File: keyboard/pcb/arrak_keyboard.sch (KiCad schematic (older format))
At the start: 40 parts, among them SW1 SW_PUSH, SW10 SW_PUSH, SW11 SW_PUSH, SW12 SW_PUSH, SW13 SW_PUSH, SW14 SW_PUSH, SW15 SW_PUSH, SW16 SW_PUSH, SW17 SW_PUSH, SW18 SW_PUSH, SW19 SW_PUSH, SW2 SW_PUSH, SW20 SW_PUSH, SW21 SW_PUSH, SW22 SW_PUSH, SW23 SW_PUSH, SW24 SW_PUSH, SW25 SW_PUSH, SW26 SW_PUSH, SW27 SW_PUSH, SW28 SW_PUSH, SW29 SW_PUSH, SW3 SW_PUSH, SW30 SW_PUSH, SW31 SW_PUSH, SW32 SW_PUSH, SW33 SW_PUSH, SW34 SW_PUSH, SW35 SW_PUSH, SW36 SW_PUSH, SW4 SW_PUSH, SW5 SW_PUSH, SW6 SW_PUSH, SW7 SW_PUSH, SW8 SW_PUSH, SW9 SW_PUSH

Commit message: weird routing
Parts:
- gave numbers to parts that had none: 4
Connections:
- net D10: now also J1.7 (Pin_7); no longer J1.9 (Pin_9)
- net D11: now also J1.15 (Pin_15); no longer J1.8 (Pin_8)
- net D12: now also J1.10 (Pin_10); no longer J1.7 (Pin_7)
- net D13: now also J1.5 (Pin_5); no longer J1.6 (Pin_6)
- net D14: now also J1.8 (Pin_8); no longer J1.5 (Pin_5)
- net D15: now also J1.14 (Pin_14); no longer J1.4 (Pin_4)
- net D17: now also J1.6 (Pin_6); no longer J1.2 (Pin_2)
- net D18: now also J1.9 (Pin_9); no longer J1.1 (Pin_1)
- net D19: now also J2.14 (Pin_14), SW19.2; no longer J2.18 (Pin_18), SW34.2
- net D2: now also J1.13 (Pin_13); no longer J1.17 (Pin_17)
- net D20: now also J2.10 (Pin_10), SW20.2; no longer J2.17 (Pin_17), SW35.2
- net D21: now also J2.6 (Pin_6), SW21.2; no longer J2.16 (Pin_16), SW36.2
- net D22: now also J2.3 (Pin_3), SW22.2; no longer J2.15 (Pin_15), SW31.2
- net D23: now also J2.15 (Pin_15), SW23.2; no longer J2.14 (Pin_14), SW32.2
- net D24: now also SW24.2; no longer SW33.2
- net D25: now also SW25.2; no longer SW27.2
- net D26: now also SW26.2; no longer SW28.2
- net D27: now also J2.16 (Pin_16), SW27.2; no longer J2.10 (Pin_10), SW29.2
- net D28: now also SW28.2; no longer SW30.2
- net D29: now also SW29.2; no longer SW23.2
- net D3: now also J1.1 (Pin_1); no longer J1.16 (Pin_16)
- net D30: now also SW30.2; no longer SW24.2
- net D31: now also J2.17 (Pin_17), SW31.2; no longer J2.6 (Pin_6), SW25.2
- net D32: now also SW32.2; no longer SW26.2
- net D33: now also SW33.2; no longer SW19.2
- net D34: now also J2.18 (Pin_18), SW34.2; no longer J2.3 (Pin_3), SW20.2
- net D35: now also SW35.2; no longer SW21.2
- net D36: now also SW36.2; no longer SW22.2
- net D4: now also J1.17 (Pin_17); no longer J1.15 (Pin_15)
- net D5: now also J1.12 (Pin_12); no longer J1.14 (Pin_14)
- net D6: now also J1.2 (Pin_2); no longer J1.13 (Pin_13)
- net D7: now also J1.16 (Pin_16); no longer J1.12 (Pin_12)
- net D9: now also J1.4 (Pin_4); no longer J1.10 (Pin_10)

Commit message: lite bättre routing
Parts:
- removed J3, J4: Conn_01x02_Male, symbol Connector:Conn_01x02_Male
- J1: value Conn_01x18_Male -> Conn_01x20_Male; symbol Connector:Conn_01x18_Male -> Connector:Conn_01x20_Male
- J2: value Conn_01x18_Male -> Conn_01x20_Male; footprint (none) -> Connector_PinHeader_2.54mm:PinHeader_1x20_P2.54mm_Vertical; symbol Connector:Conn_01x18_Male -> Connector:Conn_01x20_Male
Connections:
- net D16: now also J1.2 (Pin_2); no longer J1.3 (Pin_3)
- net D20: now also J2.5 (Pin_5); no longer J2.10 (Pin_10)
- net D22: now also J2.9 (Pin_9); no longer J2.3 (Pin_3)
- net D24: now also J2.10 (Pin_10); no longer J2.13 (Pin_13)
- net D25: now also J2.4 (Pin_4); no longer J2.12 (Pin_12)
- net D26: now also J2.8 (Pin_8); no longer J2.11 (Pin_11)
- net D28: now also J2.11 (Pin_11); no longer J2.9 (Pin_9)
- net D29: now also J2.3 (Pin_3); no longer J2.8 (Pin_8)
- net D32: now also J2.12 (Pin_12); no longer J2.5 (Pin_5)
- net D33: now also J2.2 (Pin_2); no longer J2.4 (Pin_4)
- net D35: now also J2.13 (Pin_13); no longer J2.2 (Pin_2)
- net D6: now also J1.3 (Pin_3); no longer J1.2 (Pin_2)
- net R1: now also J1.20 (Pin_20)
- net R2: now also J1.19 (Pin_19)
- net R3: now also J2.20 (Pin_20)
- net R4: now also J2.19 (Pin_19)
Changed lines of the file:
@@
 Text GLabel 4150 2200 0    50   Input ~ 0
 R4
-Text GLabel 7300 1150 3    50   Input ~ 0
+Text GLabel 5100 1150 3    50   Input ~ 0
 R1
-Text GLabel 7400 1150 3    50   Input ~ 0
+Text GLabel 5200 1150 3    50   Input ~ 0
 R2
-Text GLabel 7300 3000 3    50   Input ~ 0
+Text GLabel 5000 3050 3    50   Input ~ 0
 R3
-Text GLabel 7400 3000 3    50   Input ~ 0
+Text GLabel 5100 3050 3    50   Input ~ 0
 R4
-Text GLabel 5100 1150 3    50   Input ~ 0
+Text GLabel 5300 1150 3    50   Input ~ 0
 D1
+Text GLabel 5800 1150 3    50   Input ~ 0
+D2
+Text GLabel 7000 1150 3    50   Input ~ 0
+D3
+Text GLabel 5400 1150 3    50   Input ~ 0
+D4
+Text GLabel 5900 1150 3    50   Input ~ 0
+D5
+Text GLabel 5500 1150 3    50   Input ~ 0
+D7
+Text GLabel 6000 1150 3    50   Input ~ 0
+D8
+Text GLabel 6700 1150 3    50   Input ~ 0
+D9
+Text GLabel 6400 1150 3    50   Input ~ 0
+D10
 Text GLabel 5600 1150 3    50   Input ~ 0
-D2
-Text GLabel 6800 1150 3    50   Input ~ 0
-D3
-Text GLabel 5200 1150 3    50   Input ~ 0
-D4
+D11
+Text GLabel 6100 1150 3    50   Input ~ 0
+D12
+Text GLabel 6600 1150 3    50   Input ~ 0
+D13
+Text GLabel 6300 1150 3    50   Input ~ 0
+D14
 Text GLabel 5700 1150 3    50   Input ~ 0
-D5
-Text GLabel 5300 1150 3    50   Input ~ 0
-D7
-Text GLabel 5800 1150 3    50   Input ~ 0
-D8
+D15
+Text GLabel 6900 1150 3    50   Input ~ 0
+D16
 Text GLabel 6500 1150 3    50   Input ~ 0
-D9
+D17
 Text GLabel 6200 1150 3    50   Input ~ 0
-D10
-Text GLabel 5400 1150 3    50   Input ~ 0
-D11
-Text GLabel 5900 1150 3    50   Input ~ 0
-D12
-Text GLabel 6400 1150 3    50   Input ~ 0
-D13
-Text GLabel 6100 1150 3    50   Input ~ 0
-D14
-Text GLabel 5500 1150 3    50   Input ~ 0
-D15
-Text GLabel 6600 1150 3    50   Input ~ 0
-D16
-Text GLabel 6300 1150 3    50   Input ~ 0
-D17
-Text GLabel 6000 1150 3    50   Input ~ 0
 D18
 Entry Wire Line
@@
 Text GLabel 2500 4100 0    50   Input ~ 0
 R4
-Text GLabel 6700 1150 3    50   Input ~ 0
+Text GLabel 6800 1150 3    50   Input ~ 0
 D6
 $Comp
-L Connector:Conn_01x18_Male J1
+L Connector:Conn_01x20_Male J1
 U 1 1 6117D25B
-P 6000 950
-F 0 "J1" V 5835 878 50  0000 C CNN
-F 1 "Conn_01x18_Male" V 5926 878 50  0000 C CNN
-F 2 "" H 6000 950 50  0001 C CNN
-F 3 "~" H 6000 950 50  0001 C CNN
-	1    6000 950
+P 6100 950
+F 0 "J1" V 5935 878 50  0000 C CNN
+F 1 "Conn_01x20_Male" V 6026 878 50  0000 C CNN
+F 2 "" H 6100 950 50  0001 C CNN
+F 3 "~" H 6100 950 50  0001 C CNN
+	1    6100 950
 	0    1    1    0
 $EndComp
 $Comp
-L Connector:Conn_01x18_Male J2
+L Connector:Conn_01x20_Male J2
 U 1 1 6117F46E
 P 6000 2850
 F 0 "J2" V 5835 2778 50  0000 C CNN
-F 1 "Conn_01x18_Male" V 5926 2778 50  0000 C CNN
-F 2 "" H 6000 2850 50  0001 C CNN
+F 1 "Conn_01x20_Male" V 5926 2778 50  0000 C CNN
+F 2 "Connector_PinHeader_2.54mm:PinHeader_1x20_P2.54mm_Vertical" H 6000 2850 50  0001 C CNN
 F 3 "~" H 6000 2850 50  0001 C CNN
 	1    6000 2850
-	0    1    1    0
-$EndComp
-$Comp
-L Connector:Conn_01x02_Male J3
-U 1 1 61180CFF
-P 7400 950
-F 0 "J3" V 7462 994 50  0000 L CNN
-F 1 "Conn_01x02_Male" V 7553 994 50  0000 L CNN
-F 2 "" H 7400 950 50  0001 C CNN
-F 3 "~" H 7400 950 50  0001 C CNN
-	1    7400 950
-	0    1    1    0
-$EndComp
-$Comp
-L Connector:Conn_01x02_Male J4
-U 1 1 6118151C
-P 7400 2800
-F 0 "J4" V 7462 2844 50  0000 L CNN
-F 1 "Conn_01x02_Male" V 7553 2844 50  0000 L CNN
-F 2 "" H 7400 2800 50  0001 C CNN
-F 3 "~" H 7400 2800 50  0001 C CNN
-	1    7400 2800
 	0    1    1    0
 $EndComp
@@
 Text GLabel 4800 3700 3    50   Input ~ 0
 D36
+Text GLabel 5600 3050 3    50   Input ~ 0
+D19
+Text GLabel 6500 3050 3    50   Input ~ 0
+D20
+Text GLabel 6400 3050 3    50   Input ~ 0
+D21
+Text GLabel 6100 3050 3    50   Input ~ 0
+D22
 Text GLabel 5500 3050 3    50   Input ~ 0
-D19
+D23
+Text GLabel 6000 3050 3    50   Input ~ 0
+D24
+Text GLabel 6600 3050 3    50   Input ~ 0
+D25
+Text GLabel 6200 3050 3    50   Input ~ 0
+D26
+Text GLabel 5400 3050 3    50   Input ~ 0
+D27
 Text GLabel 5900 3050 3    50   Input ~ 0
-D20
+D28
+Text GLabel 6700 3050 3    50   Input ~ 0
+D29
 Text GLabel 6300 3050 3    50   Input ~ 0
-D21
-Text GLabel 6600 3050 3    50   Input ~ 0
-D22
-Text GLabel 5400 3050 3    50   Input ~ 0
-D23
-Text GLabel 5600 3050 3    50   Input ~ 0
-D24
+D30
+Text GLabel 5300 3050 3    50   Input ~ 0
+D31
+Text GLabel 5800 3050 3    50   Input ~ 0
+D32
+Text GLabel 6800 3050 3    50   Input ~ 0
+D33
+Text GLabel 5200 3050 3    50   Input ~ 0
+D34
 Text GLabel 5700 3050 3    50   Input ~ 0
-D25
-Text GLabel 5800 3050 3    50   Input ~ 0
-D26
-Text GLabel 5300 3050 3    50   Input ~ 0
-D27
-Text GLabel 6000 3050 3    50   Input ~ 0
-D28
-Text GLabel 6100 3050 3    50   Input ~ 0
-D29
-Text GLabel 6200 3050 3    50   Input ~ 0
-D30
-Text GLabel 5200 3050 3    50   Input ~ 0
-D31
-Text GLabel 6400 3050 3    50   Input ~ 0
-D32
-Text GLabel 6500 3050 3    50   Input ~ 0
-D33
-Text GLabel 5100 3050 3    50   Input ~ 0
-D34
-Text GLabel 6700 3050 3    50   Input ~ 0
 D35
-Text GLabel 6800 3050 3    50   Input ~ 0
+Text GLabel 6900 3050 3    50   Input ~ 0
 D36
 $Comp

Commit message: finish keyboard pcb
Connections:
- net D10: now also J1.9 (Pin_9); no longer J1.7 (Pin_7)
- net D11: now also J1.5 (Pin_5); no longer J1.15 (Pin_15)
- net D12: now also J1.6 (Pin_6); no longer J1.10 (Pin_10)
- net D13: now also J1.7 (Pin_7); no longer J1.5 (Pin_5)
- net D15: now also J1.1 (Pin_1); no longer J1.14 (Pin_14)
- net D17: now also J1.3 (Pin_3); no longer J1.6 (Pin_6)
- net D18: now also J1.4 (Pin_4); no longer J1.9 (Pin_9)
- net D19: now also J2.1 (Pin_1); no longer J2.14 (Pin_14)
- net D2: now also J1.17 (Pin_17); no longer J1.13 (Pin_13)
- net D20: now also J2.2 (Pin_2); no longer J2.5 (Pin_5)
- net D21: now also J2.3 (Pin_3); no longer J2.6 (Pin_6)
- net D22: now also J2.4 (Pin_4); no longer J2.9 (Pin_9)
- net D23: now also J2.5 (Pin_5); no longer J2.15 (Pin_15)
- net D24: now also J2.6 (Pin_6); no longer J2.10 (Pin_10)
- net D25: now also J2.7 (Pin_7); no longer J2.4 (Pin_4)
- net D27: now also J2.12 (Pin_12); no longer J2.16 (Pin_16)
- net D29: now also J2.10 (Pin_10); no longer J2.3 (Pin_3)
- net D3: now also J1.16 (Pin_16); no longer J1.1 (Pin_1)
- net D30: now also J2.9 (Pin_9); no longer J2.7 (Pin_7)
- net D31: now also J2.15 (Pin_15); no longer J2.17 (Pin_17)
- net D32: now also J2.14 (Pin_14); no longer J2.12 (Pin_12)
- net D33: now also J2.13 (Pin_13); no longer J2.2 (Pin_2)
- net D35: now also J2.17 (Pin_17); no longer J2.13 (Pin_13)
- net D36: now also J2.16 (Pin_16); no longer J2.1 (Pin_1)
- net D4: now also J1.15 (Pin_15); no longer J1.17 (Pin_17)
- net D5: now also J1.14 (Pin_14); no longer J1.12 (Pin_12)
- net D6: now also J1.13 (Pin_13); no longer J1.3 (Pin_3)
- net D7: now also J1.12 (Pin_12); no longer J1.16 (Pin_16)
- net D9: now also J1.10 (Pin_10); no longer J1.4 (Pin_4)
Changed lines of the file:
@@
 Text GLabel 5300 1150 3    50   Input ~ 0
 D1
-Text GLabel 5800 1150 3    50   Input ~ 0
+Text GLabel 5400 1150 3    50   Input ~ 0
 D2
-Text GLabel 7000 1150 3    50   Input ~ 0
+Text GLabel 5500 1150 3    50   Input ~ 0
 D3
-Text GLabel 5400 1150 3    50   Input ~ 0
+Text GLabel 5600 1150 3    50   Input ~ 0
 D4
+Text GLabel 5700 1150 3    50   Input ~ 0
+D5
 Text GLabel 5900 1150 3    50   Input ~ 0
-D5
-Text GLabel 5500 1150 3    50   Input ~ 0
 D7
 Text GLabel 6000 1150 3    50   Input ~ 0
 D8
-Text GLabel 6700 1150 3    50   Input ~ 0
+Text GLabel 6100 1150 3    50   Input ~ 0
 D9
+Text GLabel 6200 1150 3    50   Input ~ 0
+D10
+Text GLabel 6600 1150 3    50   Input ~ 0
+D11
+Text GLabel 6500 1150 3    50   Input ~ 0
+D12
 Text GLabel 6400 1150 3    50   Input ~ 0
-D10
-Text GLabel 5600 1150 3    50   Input ~ 0
-D11
-Text GLabel 6100 1150 3    50   Input ~ 0
-D12
-Text GLabel 6600 1150 3    50   Input ~ 0
 D13
 Text GLabel 6300 1150 3    50   Input ~ 0
 D14
-Text GLabel 5700 1150 3    50   Input ~ 0
+Text GLabel 7000 1150 3    50   Input ~ 0
 D15
 Text GLabel 6900 1150 3    50   Input ~ 0
 D16
-Text GLabel 6500 1150 3    50   Input ~ 0
+Text GLabel 6800 1150 3    50   Input ~ 0
 D17
-Text GLabel 6200 1150 3    50   Input ~ 0
+Text GLabel 6700 1150 3    50   Input ~ 0
 D18
-Entry Wire Line
-	1200 1200 1300 1300
 Text GLabel 800  2900 0    50   Input ~ 0
 R1
@@
 Text GLabel 2500 4100 0    50   Input ~ 0
 R4
-Text GLabel 6800 1150 3    50   Input ~ 0
+Text GLabel 5800 1150 3    50   Input ~ 0
 D6
 $Comp
@@
 Text GLabel 4800 3700 3    50   Input ~ 0
 D36
-Text GLabel 5600 3050 3    50   Input ~ 0
+Text GLabel 6900 3050 3    50   Input ~ 0
 D19
+Text GLabel 6800 3050 3    50   Input ~ 0
+D20
+Text GLabel 6700 3050 3    50   Input ~ 0
+D21
+Text GLabel 6600 3050 3    50   Input ~ 0
+D22
 Text GLabel 6500 3050 3    50   Input ~ 0
-D20
+D23
 Text GLabel 6400 3050 3    50   Input ~ 0
-D21
-Text GLabel 6100 3050 3    50   Input ~ 0
-D22
-Text GLabel 5500 3050 3    50   Input ~ 0
-D23
-Text GLabel 6000 3050 3    50   Input ~ 0
 D24
-Text GLabel 6600 3050 3    50   Input ~ 0
+Text GLabel 6300 3050 3    50   Input ~ 0
 D25
 Text GLabel 6200 3050 3    50   Input ~ 0
 D26
-Text GLabel 5400 3050 3    50   Input ~ 0
+Text GLabel 5800 3050 3    50   Input ~ 0
 D27
 Text GLabel 5900 3050 3    50   Input ~ 0
 D28
-Text GLabel 6700 3050 3    50   Input ~ 0
+Text GLabel 6000 3050 3    50   Input ~ 0
 D29
-Text GLabel 6300 3050 3    50   Input ~ 0
+Text GLabel 6100 3050 3    50   Input ~ 0
 D30
-Text GLabel 5300 3050 3    50   Input ~ 0
+Text GLabel 5500 3050 3    50   Input ~ 0
 D31
-Text GLabel 5800 3050 3    50   Input ~ 0
+Text GLabel 5600 3050 3    50   Input ~ 0
 D32
-Text GLabel 6800 3050 3    50   Input ~ 0
+Text GLabel 5700 3050 3    50   Input ~ 0
 D33
 Text GLabel 5200 3050 3    50   Input ~ 0
 D34
-Text GLabel 5700 3050 3    50   Input ~ 0
+Text GLabel 5300 3050 3    50   Input ~ 0
 D35
-Text GLabel 6900 3050 3    50   Input ~ 0
+Text GLabel 5400 3050 3    50   Input ~ 0
 D36
 $Comp

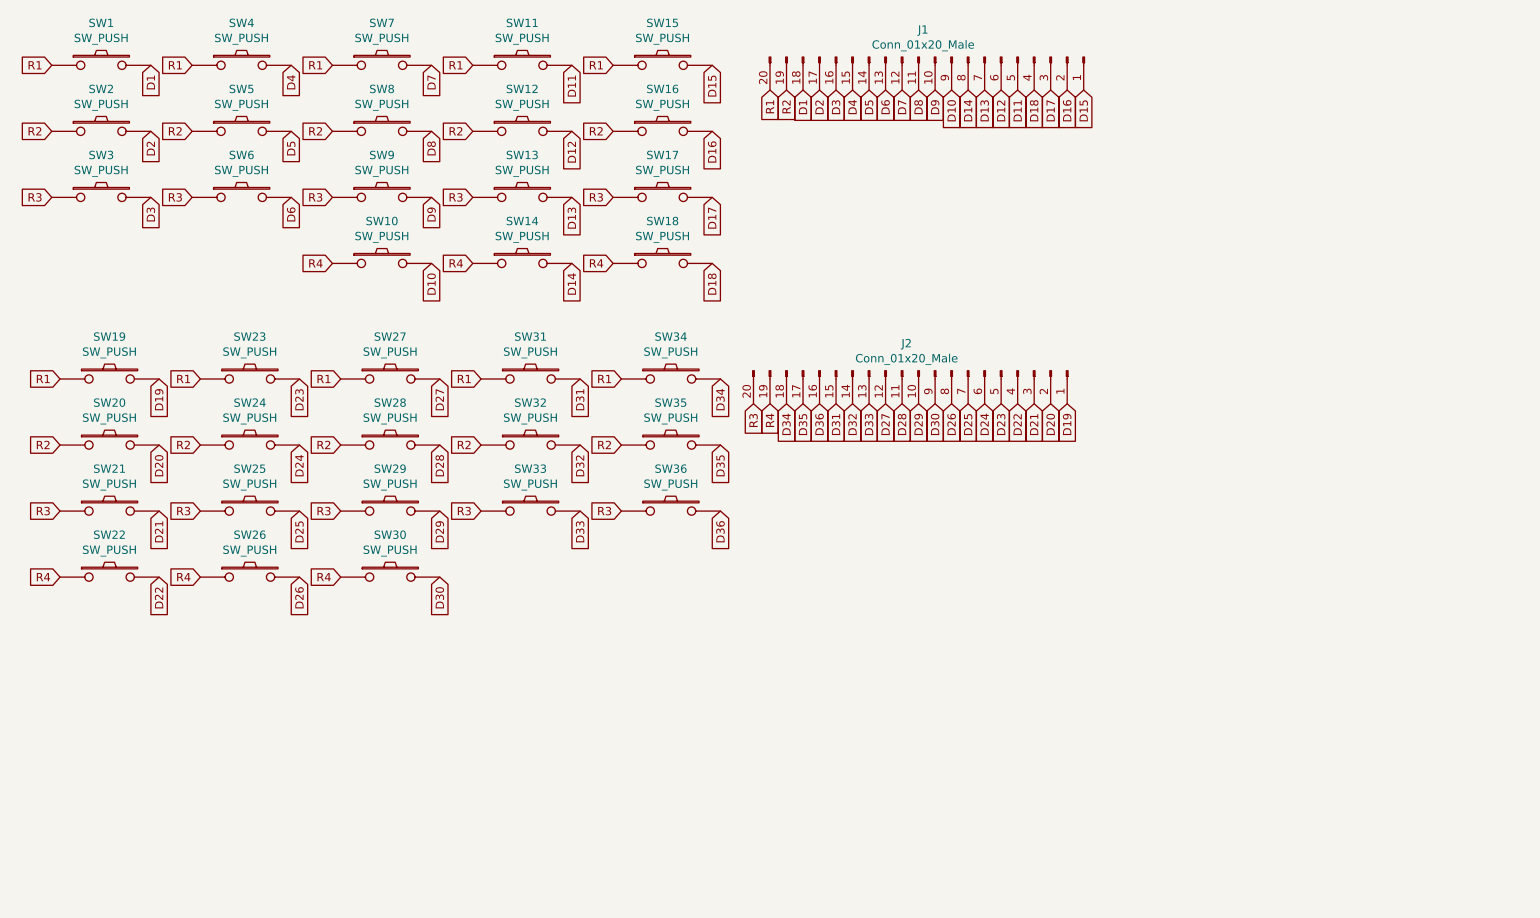
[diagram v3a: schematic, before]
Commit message: routing on wf module done
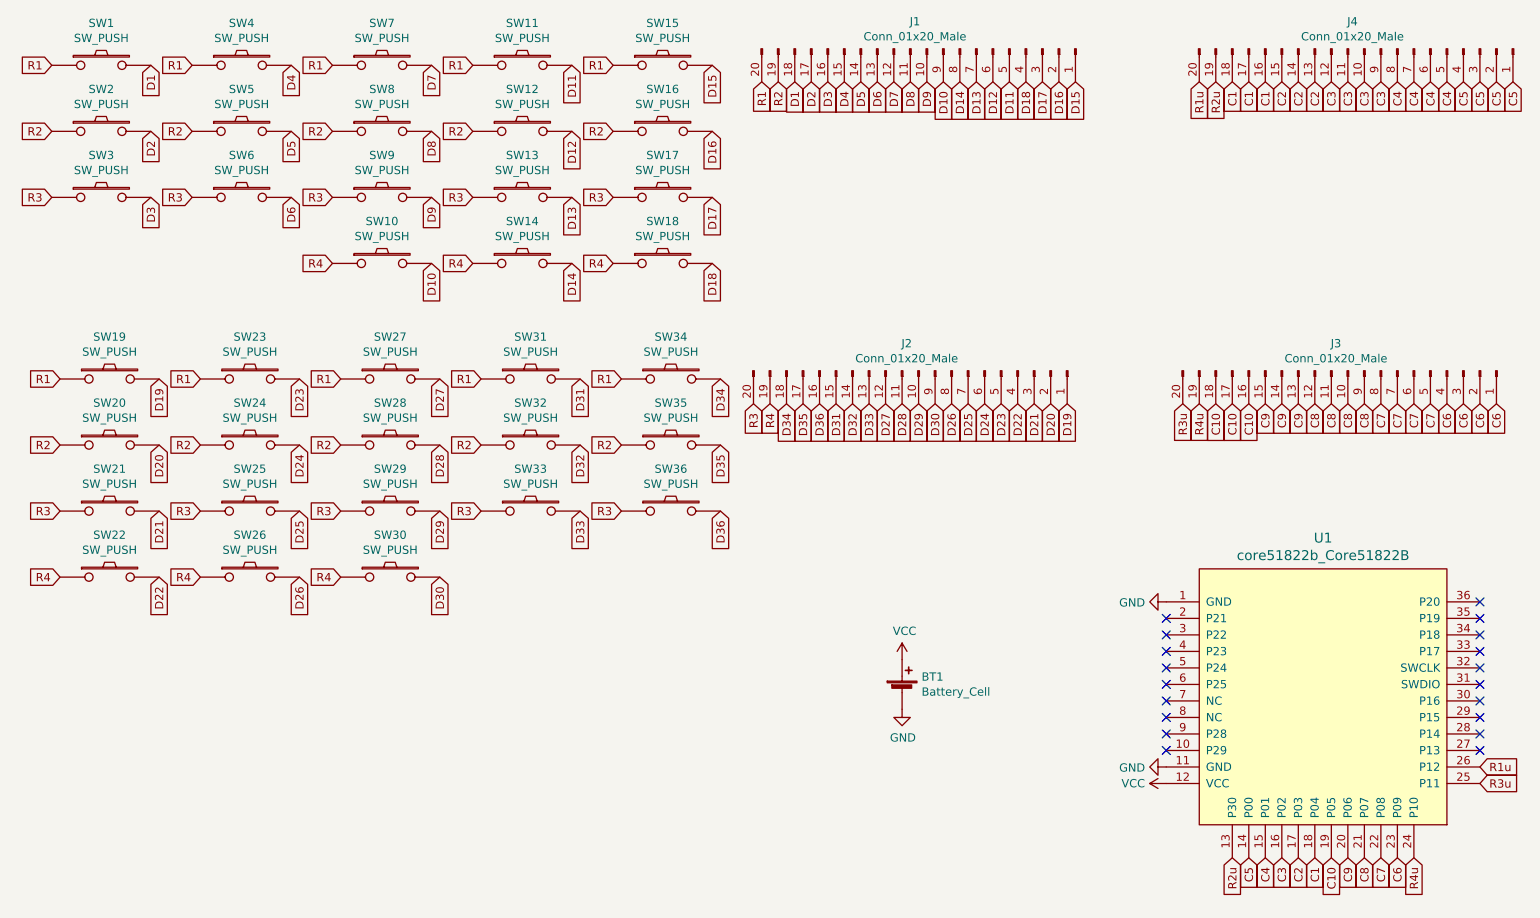
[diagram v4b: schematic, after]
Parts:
- added BT1: Battery_Cell, Battery:BatteryHolder_Keystone_3034_1x20mm, symbol Device:Battery_Cell
- added J3, J4: Conn_01x20_Male, Connector_PinHeader_2.54mm:PinHeader_1x20_P2.54mm_Vertical, symbol Connector:Conn_01x20_Male
- added U1: core51822b_Core51822B, redox_w_footprints:MY-YJ-14015-Module, symbol redox_rev1-cache:core51822b_Core51822B
- J1: footprint (none) -> Connector_PinHeader_2.54mm:PinHeader_1x20_P2.54mm_Vertical
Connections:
- new net C1: J4.16 (Pin_16), J4.17 (Pin_17), J4.18 (Pin_18), U1.18 (P04)
- new net C10: J3.16 (Pin_16), J3.17 (Pin_17), J3.18 (Pin_18), U1.19 (P05)
- new net C2: J4.13 (Pin_13), J4.14 (Pin_14), J4.15 (Pin_15), U1.17 (P03)
- new net C3: J4.10 (Pin_10), J4.11 (Pin_11), J4.12 (Pin_12), J4.9 (Pin_9), U1.16 (P02)
- new net C4: J4.5 (Pin_5), J4.6 (Pin_6), J4.7 (Pin_7), J4.8 (Pin_8), U1.15 (P01)
- new net C5: J4.1 (Pin_1), J4.2 (Pin_2), J4.3 (Pin_3), J4.4 (Pin_4), U1.14 (P00)
- new net C6: J3.1 (Pin_1), J3.2 (Pin_2), J3.3 (Pin_3), J3.4 (Pin_4), U1.23 (P09)
- new net C7: J3.5 (Pin_5), J3.6 (Pin_6), J3.7 (Pin_7), J3.8 (Pin_8), U1.22 (P08)
- new net C8: J3.10 (Pin_10), J3.11 (Pin_11), J3.12 (Pin_12), J3.9 (Pin_9), U1.21 (P07)
- new net C9: J3.13 (Pin_13), J3.14 (Pin_14), J3.15 (Pin_15), U1.20 (P06)
- new net GND: BT1.2 (-), U1.1 (GND), U1.11 (GND)
- new net R1u: J4.20 (Pin_20), U1.26 (P12)
- new net R2u: J4.19 (Pin_19), U1.13 (P30)
- new net R3u: J3.20 (Pin_20), U1.25 (P11)
- new net R4u: J3.19 (Pin_19), U1.24 (P10)
- new net VCC: BT1.1 (+), U1.12 (VCC)
- no-connect marks 0 -> 19
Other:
- moved on the sheet: J1
